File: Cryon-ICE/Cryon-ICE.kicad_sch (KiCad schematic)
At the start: 2 parts, among them J101 Conn_02x32_Row_Letter_First, U101 MPFS025T-FCVG484I

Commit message: Added micro-sd to schematic
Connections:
- net SD_DET: now reaches U101.C7 (GPIO39NB1)
- net eMMC_SD/ADC_MISO: now reaches U101.A2 (MSSIO33B2)
- net eMMC_SD/ADC_MOSI: now reaches U101.B2 (MSSIO32B2)
- net eMMC_SD/ADC_SCK: now reaches U101.E5 (MSSIO30B2)
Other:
- added sheet eMMC_SD (eMMC_SD.kicad_sch)
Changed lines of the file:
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@@
 	(wire
 		(pts
+			(xy 134.62 200.66) (xy 182.88 200.66)
+		)
+		(stroke
+			(width 0)
+			(type default)
+		)
+	)
+	(wire
+		(pts
+			(xy 547.37 92.71) (xy 566.42 92.71)
+		)
+		(stroke
+			(width 0)
+			(type default)
+		)
+	)
+	(wire
+		(pts
 			(xy 173.99 213.36) (xy 173.99 187.96)
 		)
@@
 	(wire
 		(pts
+			(xy 156.21 195.58) (xy 156.21 198.12)
+		)
+		(stroke
+			(width 0)
+			(type default)
+		)
+	)
+	(wire
+		(pts
 			(xy 134.62 157.48) (xy 142.24 157.48)
 		)
@@
 	(wire
 		(pts
+			(xy 134.62 203.2) (xy 182.88 203.2)
+		)
+		(stroke
+			(width 0)
+			(type default)
+		)
+	)
+	(wire
+		(pts
 			(xy 134.62 160.02) (xy 142.24 160.02)
 		)
@@
 	(wire
 		(pts
+			(xy 156.21 198.12) (xy 182.88 198.12)
+		)
+		(stroke
+			(width 0)
+			(type default)
+		)
+	)
+	(wire
+		(pts
 			(xy 33.02 60.96) (xy 42.672 60.96)
 		)
@@
 	(wire
 		(pts
+			(xy 160.02 227.33) (xy 182.88 227.33)
+		)
+		(stroke
+			(width 0)
+			(type default)
+		)
+	)
+	(wire
+		(pts
 			(xy 163.83 185.42) (xy 164.084 185.42)
 		)
@@
 	(wire
 		(pts
+			(xy 134.62 195.58) (xy 156.21 195.58)
+		)
+		(stroke
+			(width 0)
+			(type default)
+		)
+	)
+	(wire
+		(pts
 			(xy 71.12 41.91) (xy 83.82 41.91)
 		)
@@
 		)
 	)
+	(label "SD_DET"
+		(at 566.42 92.71 180)
+		(effects
+			(font
+				(size 1.27 1.27)
+			)
+			(justify right bottom)
+		)
+	)
 	(label "USB0_RESETB"
 		(at 167.64 185.42 0)
@@
 		)
 	)
+	(label "SD_DET"
+		(at 166.37 227.33 180)
+		(effects
+			(font
+				(size 1.27 1.27)
+			)
+			(justify right bottom)
+		)
+	)
 	(symbol
 		(lib_name "MPFS025T-FCVG484I_2")
@@
 		)
 		(property "Sheetfile" "USB Interface.kicad_sch"
-			(at 142.494 194.564 0)
+			(at 141.986 192.786 0)
 			(show_name no)
 			(do_not_autoplace no)
@@
 				)
 			)
+		)
+	)
+	(sheet
+		(at 182.88 194.31)
+		(size 27.94 48.26)
+		(exclude_from_sim no)
+		(in_bom yes)
+		(on_board yes)
+		(dnp no)
+		(fields_autoplaced yes)
+		(stroke
+			(width 0.1524)
+			(type solid)
+		)
+		(fill
+			(color 0 0 0 0)
+		)
+		(property "Sheetname" "eMMC_SD"
+			(at 182.88 193.5984 0)
+			(show_name no)
+			(do_not_autoplace no)
+			(effects
+				(font
+					(size 1.27 1.27)
+				)
+				(justify left bottom)
+			)
+		)
+		(property "Sheetfile" "eMMC_SD.kicad_sch"
+			(at 182.88 243.1546 0)
+			(show_name no)
+			(do_not_autoplace no)
+			(effects
+				(font
+					(size 1.27 1.27)
+				)
+				(justify left top)
+			)
+		)
+		(pin "ADC_MISO" output
+			(at 182.88 203.2 180)
+			(effects
+				(font
+					(size 1.27 1.27)
+				)
+				(justify left)
+			)
+		)
+		(pin "ADC_MOSI" input
+			(at 182.88 200.66 180)
+			(effects
+				(font
+					(size 1.27 1.27)
+				)
+				(justify left)
+			)
+		)
+		(pin "ADC_SCK" input
+			(at 182.88 198.12 180)
+			(effects
+				(font
+					(size 1.27 1.27)
+				)
+				(justify left)
+			)
+		)
+		(pin "ADC_SCK_1" output
+			(at 182.88 222.25 180)
+			(effects
+				(font
+					(size 1.27 1.27)
+				)
+				(justify left)
+			)
+		)
+		(pin "SD_DET" output
+			(at 182.88 227.33 180)
+			(effects
+				(font
+					(size 1.27 1.27)
+				)
+				(justify left)
+			)
+		)
+		(instances
+			(project "Cryon-ICE"
+				(path "/96e1c255-c0ff-457d-9e19-0aca2ce5c65e"
+					(page "7")
+				)
+			)

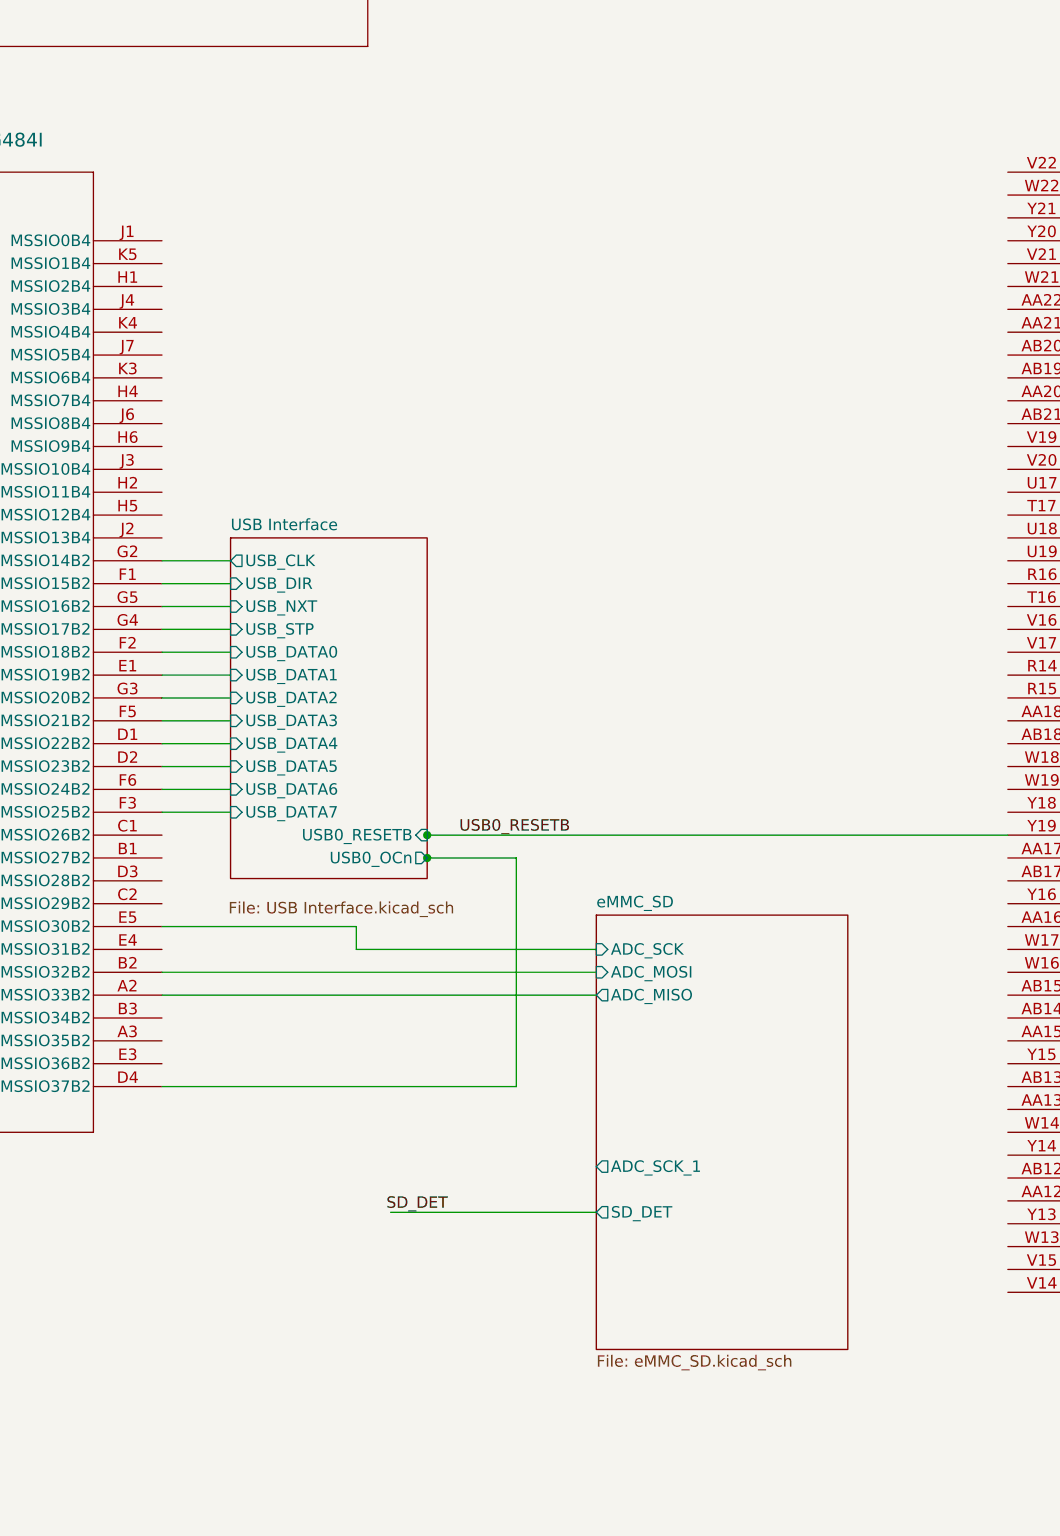
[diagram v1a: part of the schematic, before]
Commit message: Added eMMC
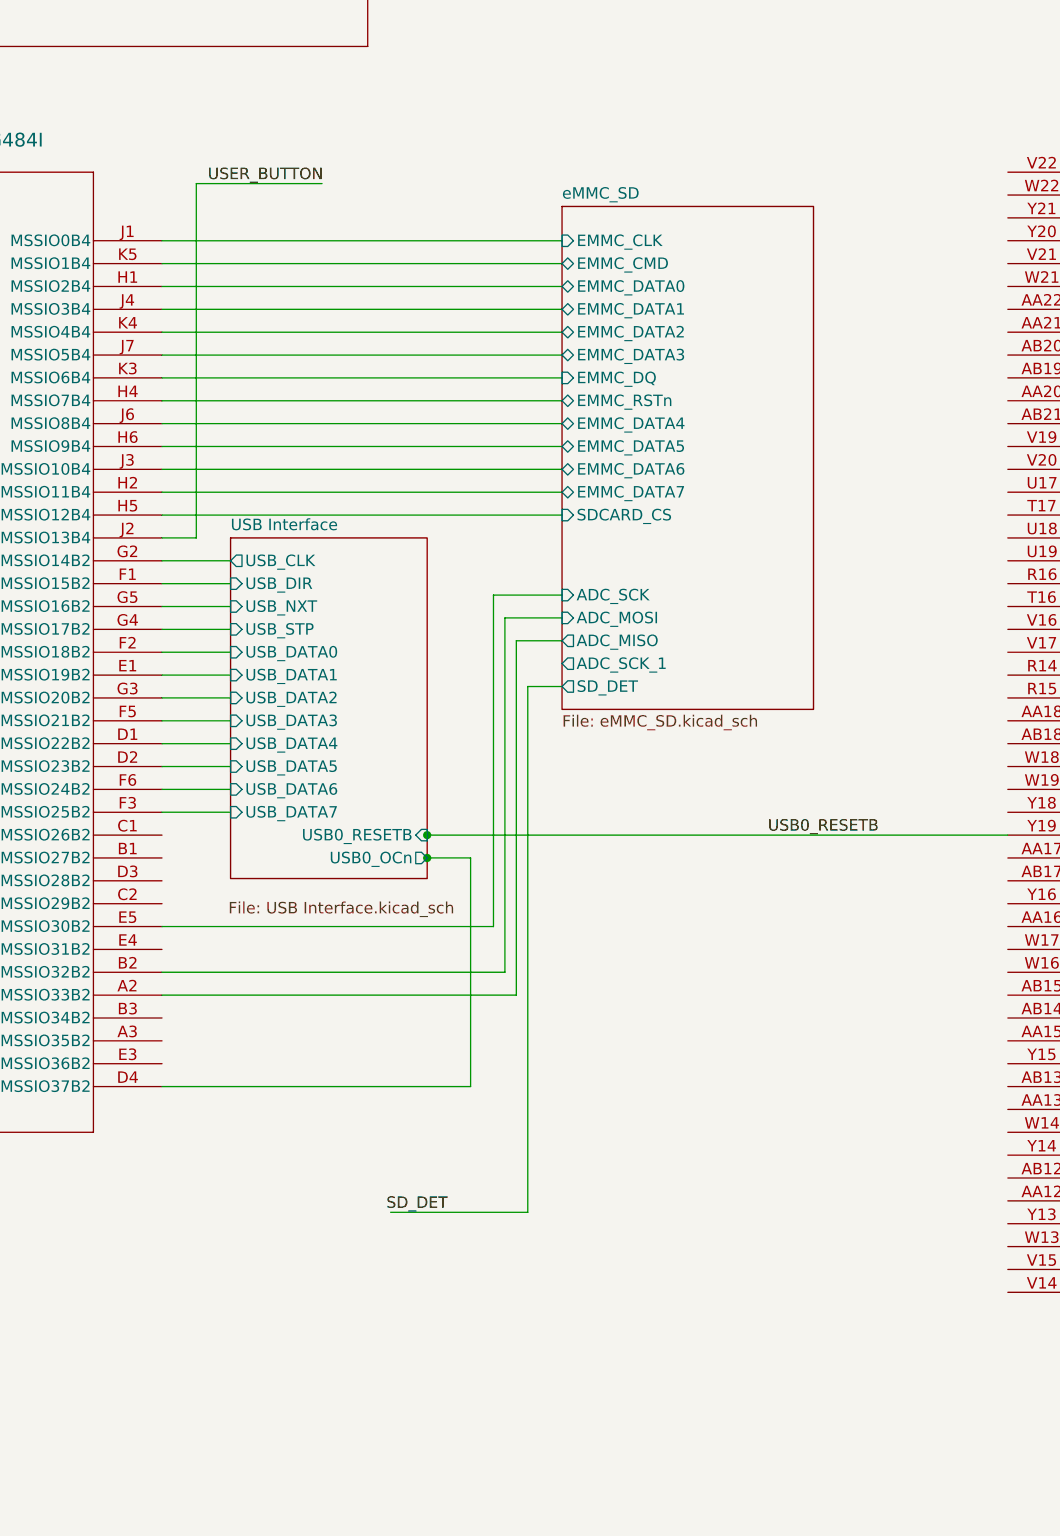
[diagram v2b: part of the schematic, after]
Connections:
- net eMMC_SD/EMMC_DATA0: now reaches U101.H1 (MSSIO2B4)
- net eMMC_SD/EMMC_DATA7: now reaches U101.H2 (MSSIO11B4)
- net eMMC_SD/EMMC_RSTn: now reaches U101.H4 (MSSIO7B4)
- net eMMC_SD/SDCARD_CS: now reaches U101.H5 (MSSIO12B4)
- net eMMC_SD/EMMC_DATA5: now reaches U101.H6 (MSSIO9B4)
- net eMMC_SD/EMMC_CLK: now reaches U101.J1 (MSSIO0B4)
- net USER_BUTTON: now reaches U101.J2 (MSSIO13B4)
- net eMMC_SD/EMMC_DATA6: now reaches U101.J3 (MSSIO10B4)
- net eMMC_SD/EMMC_DATA1: now reaches U101.J4 (MSSIO3B4)
- net eMMC_SD/EMMC_DATA4: now reaches U101.J6 (MSSIO8B4)
- net eMMC_SD/EMMC_DATA3: now reaches U101.J7 (MSSIO5B4)
- net eMMC_SD/EMMC_DQ: now reaches U101.K3 (MSSIO6B4)
- net eMMC_SD/EMMC_DATA2: now reaches U101.K4 (MSSIO4B4)
- net eMMC_SD/EMMC_CMD: now reaches U101.K5 (MSSIO1B4)
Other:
- sheet eMMC_SD ports: added EMMC_CLK, EMMC_CMD, EMMC_DATA0, EMMC_DATA1, EMMC_DATA2, EMMC_DATA3, EMMC_DATA4, EMMC_DATA5, EMMC_DATA6, EMMC_DATA7, EMMC_DQ, EMMC_RSTn, SDCARD_CS; removed none
